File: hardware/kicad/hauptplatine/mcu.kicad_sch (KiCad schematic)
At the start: 31 parts, among them J301 USB-C, J302 Debug (SWD + Serial1), SW301 Reset, SW302 BOOT, SW303 Service, SW304 Reedkontakt, U301 STM32F411CEU6, U302 USBLC6-2SC6, Y301 25MHz 12pF, Y302 32,768k 7pF

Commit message: update
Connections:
- net DBG_RX: now also J302.7 (Pin_7); no longer J302.6 (Pin_6)
- net DBG_TX: now also J302.6 (Pin_6); no longer J302.5 (Pin_5)
- net GND: now also J302.5 (Pin_5); no longer J302.7 (Pin_7)
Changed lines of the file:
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@@
 	(wire
 		(pts
-			(xy 289.56 124.46) (xy 299.72 124.46)
+			(xy 289.56 127) (xy 299.72 127)
 		)
 		(stroke
@@
 	(wire
 		(pts
-			(xy 289.56 121.92) (xy 299.72 121.92)
+			(xy 289.56 124.46) (xy 299.72 124.46)
 		)
 		(stroke
@@
 	)
 	(label "DBG_TX"
-		(at 289.56 121.92 180)
+		(at 289.56 124.46 180)
 		(effects
 			(font
@@
 	)
 	(label "DBG_RX"
-		(at 289.56 124.46 180)
+		(at 289.56 127 180)
 		(effects
 			(font
@@
 	(symbol
 		(lib_id "power:GND")
-		(at 299.72 127 270)
+		(at 299.72 121.92 270)
 		(unit 1)
 		(body_style 1)
@@
 		(dnp no)
 		(property "Reference" "#PWR3031"
-			(at 299.72 127 0)
+			(at 299.72 121.92 0)
 			(hide yes)
 			(show_name no)
@@
 		)
 		(property "Value" "GND"
-			(at 299.72 130.2 0)
+			(at 299.72 125.12 0)
 			(show_name no)
 			(do_not_autoplace no)
@@
 		)
 		(property "Footprint" ""
-			(at 299.72 127 0)
+			(at 299.72 121.92 0)
 			(hide yes)
 			(show_name no)
@@
 		)
 		(property "Datasheet" ""
-			(at 299.72 127 0)
+			(at 299.72 121.92 0)
 			(hide yes)
 			(show_name no)
@@
 		)
 		(property "Description" ""
-			(at 299.72 127 0)
+			(at 299.72 121.92 0)
 			(show_name no)
 			(do_not_autoplace no)
@@
 			)
 		)
-		(property "Description" ""
+		(property "Description" "= J10 in anschluesse.md: 1 3V3, 2 SWDIO, 3 SWCLK, 4 NRST, 5 GND, 6 TX1 (PA9, Ausgang), 7 RX1 (PA10)"
 			(at 304.8 119.38 0)
 			(hide yes)

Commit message: update
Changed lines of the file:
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@@
-		)
-	)
-	(label "DBG_TX"
-		(at 289.56 124.46 180)
-		(effects
-			(font
-				(size 1.27 1.27)
-			)
-			(justify right bottom)
 		)
 	)
@@
 		)
 	)
-	(label "DBG_TX"
-		(at 226.06 127 0)
-		(effects
-			(font
-				(size 1.27 1.27)
-			)
-			(justify left bottom)
-		)
-	)
 	(label "USB_CC1"
 		(at 292.1 214.63 90)
@@
 		)
 	)
-	(label "DBG_RX"
-		(at 226.06 129.54 0)
-		(effects
-			(font
-				(size 1.27 1.27)
-			)
-			(justify left bottom)
-		)
-	)
 	(label "VDDA"
 		(at 207.01 81.28 0)
@@
 		)
 	)
-	(label "DBG_RX"
-		(at 289.56 127 180)
-		(effects
-			(font
-				(size 1.27 1.27)
-			)
-			(justify right bottom)
-		)
-	)
 	(label "BOOT1"
 		(at 86.36 151.13 90)
@@
 		)
 	)
+	(global_label "DBG_TX"
+		(shape bidirectional)
+		(at 289.56 124.46 180)
+		(fields_autoplaced yes)
+		(effects
+			(font
+				(size 1.27 1.27)
+			)
+			(justify right)
+		)
+		(property "Intersheetrefs" "${INTERSHEET_REFS}"
+			(at 289.56 124.46 0)
+			(hide yes)
+			(show_name no)
+			(do_not_autoplace no)
+			(effects
+				(font
+					(size 1.27 1.27)
+				)
+			)
+		)
+	)
 	(global_label "LORA_NSS"
 		(shape bidirectional)
@@
 		)
 	)
+	(global_label "DBG_TX"
+		(shape bidirectional)
+		(at 226.06 127 0)
+		(fields_autoplaced yes)
+		(effects
+			(font
+				(size 1.27 1.27)
+			)
+			(justify left)
+		)
+		(property "Intersheetrefs" "${INTERSHEET_REFS}"
+			(at 226.06 127 0)
+			(hide yes)
+			(show_name no)
+			(do_not_autoplace no)
+			(effects
+				(font
+					(size 1.27 1.27)
+				)
+			)
+		)
+	)
 	(global_label "MIC_ADC"
 		(shape bidirectional)
@@
 		)
 	)
+	(global_label "DBG_RX"
+		(shape bidirectional)
+		(at 226.06 129.54 0)
+		(fields_autoplaced yes)
+		(effects
+			(font
+				(size 1.27 1.27)
+			)
+			(justify left)
+		)
+		(property "Intersheetrefs" "${INTERSHEET_REFS}"
+			(at 226.06 129.54 0)
+			(hide yes)
+			(show_name no)
+			(do_not_autoplace no)
+			(effects
+				(font
+					(size 1.27 1.27)
+				)
+			)
+		)
+	)
 	(global_label "EXT_PB13"
 		(shape bidirectional)
@@
 			(hide yes)
 			(show_name no)
+			(do_not_autoplace no)
+			(effects
+				(font
+					(size 1.27 1.27)
+				)
+			)
+		)
+	)
+	(global_label "DBG_RX"
+		(shape bidirectional)
+		(at 289.56 127 180)
+		(fields_autoplaced yes)
+		(effects
+			(font
+				(size 1.27 1.27)
+			)
+			(justify right)
+		)
+		(property "Intersheetrefs" "${INTERSHEET_REFS}"
+			(at 289.56 127 0)
+			(hide yes)
+			(show_name no)

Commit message: Update
HW-03: Distanzhülsen 10 mm, Bauhöhe ≤ 40 mm; Platinendatei logger.kicad_pcb angelegt (121×121 mm, 4 Lagen, Befestigungslöcher, DRC 0); Reedkontakt MRS03-B-3 und LED LTST-S220KGKT mit Footprints. Tests: ERC 0, Pin/Footprint 0 Abweichungen, Netzprüfung 178/178, alle_tests_linux.sh rc=0
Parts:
- D301: value Side-View -> LTST-S220KGKT; footprint LED_SMD:LED_0603_1608Metric -> Bienen:LED_Lite-On_LTST-S220_SideView; LCSC (none) -> C160469
- SW304: value Reedkontakt -> MRS03-B-3; footprint (none) -> Bienen:MiRelay_MRS03_J-Lead_8.5x2.1mm; LCSC (none) -> C41432613
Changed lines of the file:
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@@
 			)
 		)
-		(property "Value" "Reedkontakt"
+		(property "Value" "MRS03-B-3"
 			(at 256.54 76.143 0)
 			(show_name no)
@@
 			)
 		)
-		(property "Footprint" ""
+		(property "Footprint" "Bienen:MiRelay_MRS03_J-Lead_8.5x2.1mm"
 			(at 256.54 78.74 0)
 			(hide yes)
@@
 			)
 		)
-		(property "Description" "an der Platinenkante neben der LED; Teil und Footprint [P]"
+		(property "Description" "MiRelay MRS03-B-3: Reed SMD 8,5 × 2,1 mm, 10–15 AT; an der Platinenkante neben der LED, Längsachse parallel zur Kante; Schaltabstand durch die Wand am Prototyp [P]"
+			(at 256.54 78.74 0)
+			(hide yes)
+			(show_name no)
+			(do_not_autoplace no)
+			(effects
+				(font
+					(size 1.27 1.27)
+				)
+			)
+		)
+		(property "LCSC" "C41432613"
 			(at 256.54 78.74 0)
 			(hide yes)
@@
 			)
 		)
-		(property "Value" "Side-View"
+		(property "Value" "LTST-S220KGKT"
 			(at 109.966 167.081 90)
 			(show_name no)
@@
 			)
 		)
-		(property "Footprint" "LED_SMD:LED_0603_1608Metric"
+		(property "Footprint" "Bienen:LED_Lite-On_LTST-S220_SideView"
 			(at 106.68 165.1 0)
 			(hide yes)
@@
 			)
 		)
-		(property "Description" "seitlich abstrahlend am Rand unter dem Lichtleiter; Teil/Footprint [P]"
+		(property "Description" "Lite-On, seitlich abstrahlend, grün (AlInGaP 574 nm), am Rand vor dem Lichtleiter; mit 1 kΩ ca. 1,3 mA – Helligkeit am Muster prüfen [P]"
 			(at 106.68 165.1 0)
 			(hide yes)
+			(show_name no)
+			(do_not_autoplace no)
+			(effects
+				(font
+					(size 1.27 1.27)
+				)
+			)
+		)
+		(property "LCSC" "C160469"
+			(at 106.68 165.1 0)
+			(hide yes)

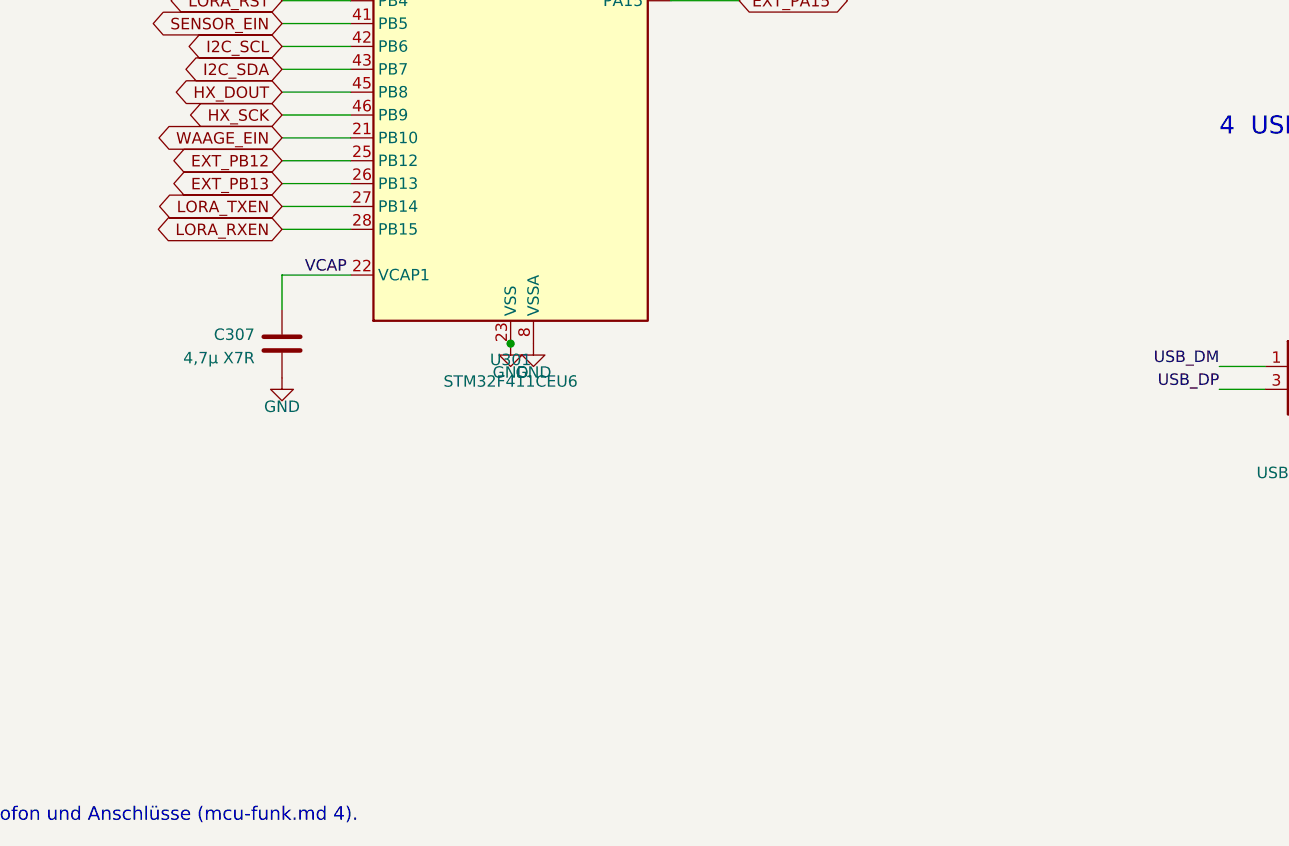
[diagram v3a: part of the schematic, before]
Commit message: HW-06: Akku auf der Hauptplatine (Blatt Akku, Akku-Platine entfällt); HW-05: USB mit VBUS-Erkennung an PB13; Routing-Werkzeuge; Aufräumen: Restbezüge Akku-Platine, README-Stand; ERC 0, Netzprüfung 168/168, Pin/Footprint 0; Platine platziert, nicht geroutet
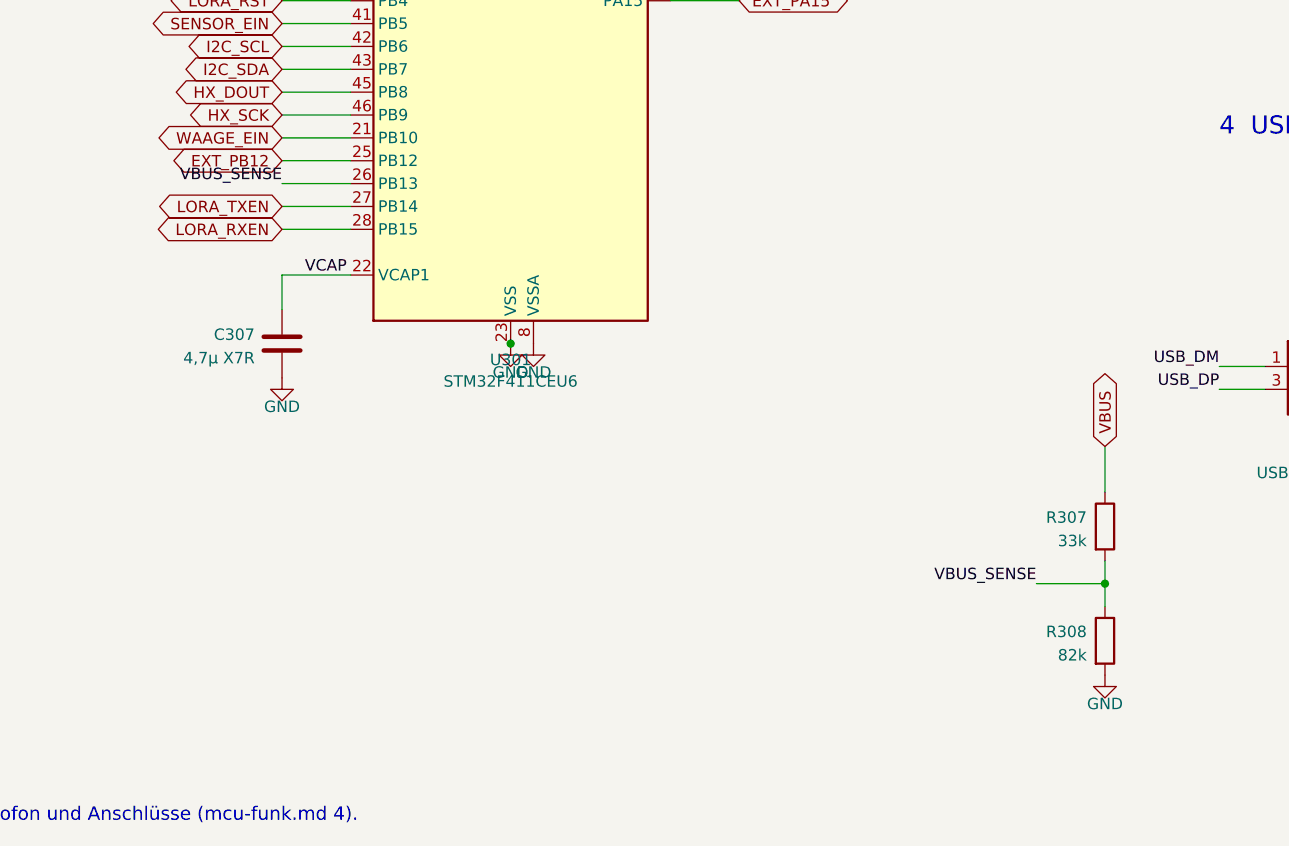
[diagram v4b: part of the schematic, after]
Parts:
- added R307: 33k, Resistor_SMD:R_0603_1608Metric, symbol Device:R
- added R308: 82k, Resistor_SMD:R_0603_1608Metric, symbol Device:R
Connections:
- net GND: now also R308.2
- net VBUS: now also R307.1
- net EXT_PB13 renamed VBUS_SENSE
- net VBUS_SENSE: now also R307.2, R308.1

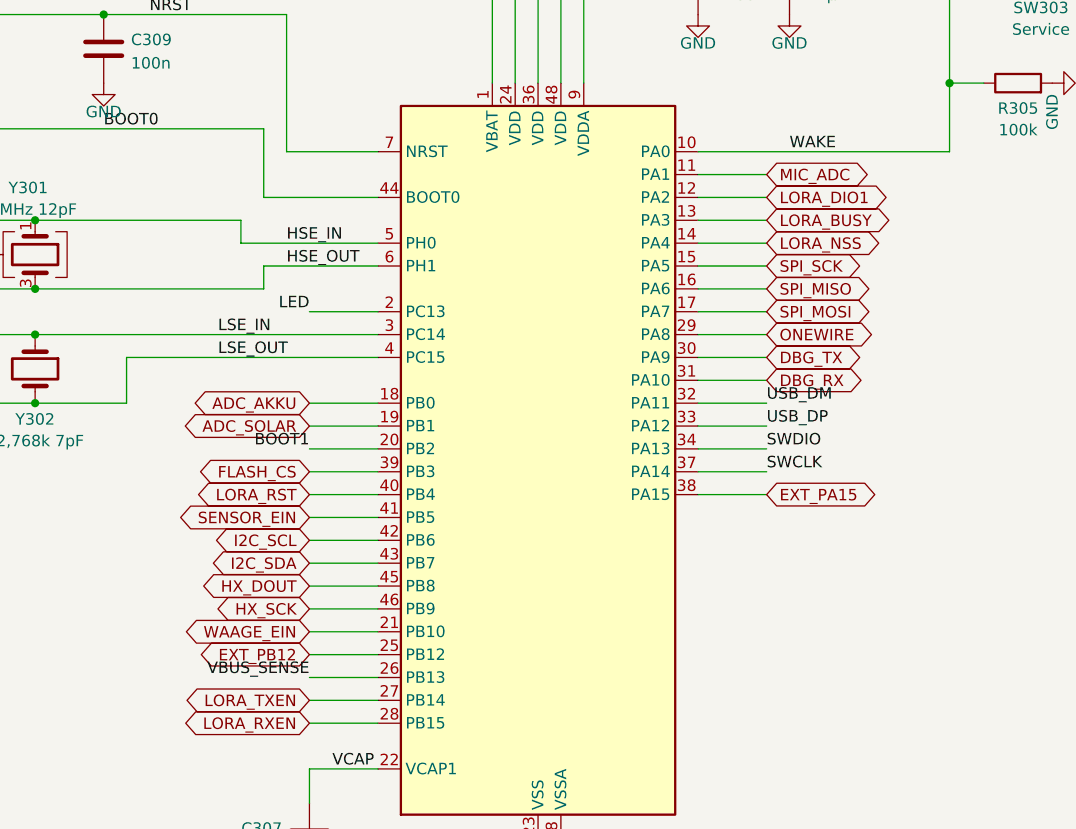
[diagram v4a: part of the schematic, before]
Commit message: HW-07: zwei Mikrofone am Audio-ADC TLV320ADC3101, I2S3, RJ45 J5; HW-08: Platine nur Rahmen, Layout extern; Pflichtenheft und Übergabepaket für den Layouter; ERC 0, Netzprüfung 187/187, Pin/Footprint 0
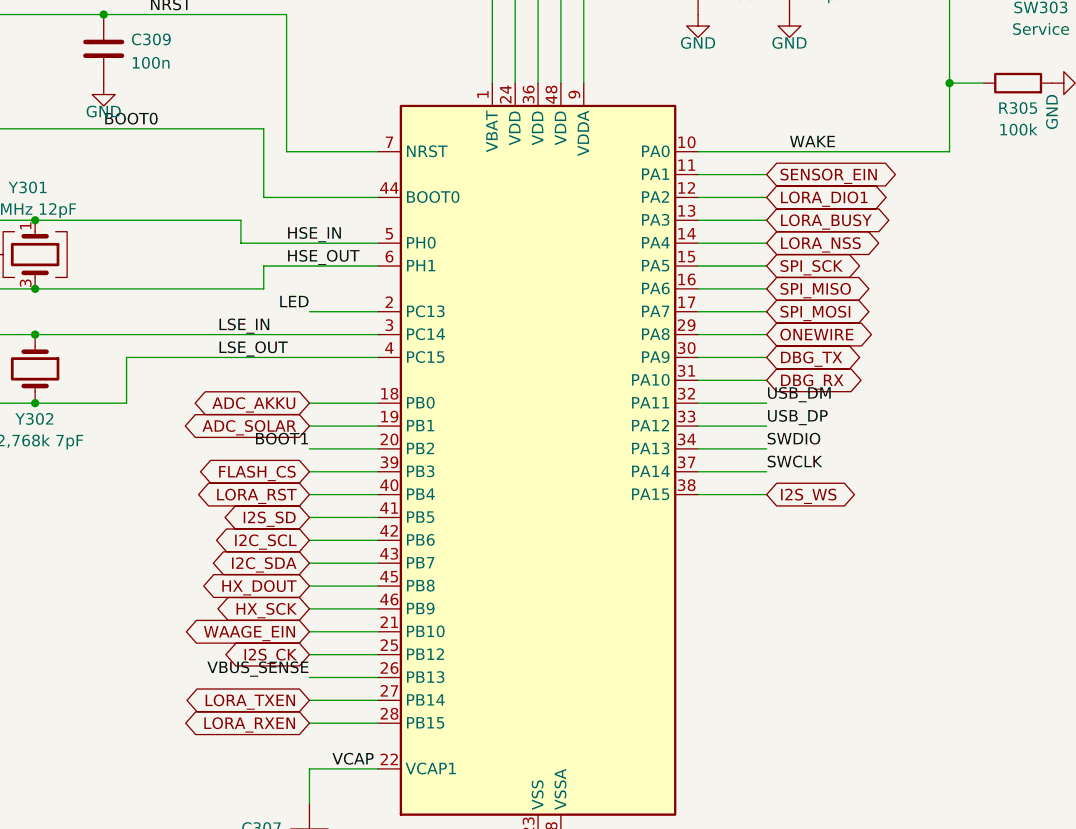
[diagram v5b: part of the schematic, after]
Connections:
- net MIC_ADC is gone; now on net SENSOR_EIN: U301.11 (PA1)
- net SENSOR_EIN: no longer U301.41 (PB5)
- net EXT_PA15 renamed I2S_WS
- net EXT_PB12 renamed I2S_CK
- new net I2S_SD: U301.41 (PB5)
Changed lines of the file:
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@@
 		)
 	)
-	(global_label "EXT_PA15"
+	(global_label "LORA_RST"
+		(shape bidirectional)
+		(at 175.26 142.24 180)
+		(fields_autoplaced yes)
+		(effects
+			(font
+				(size 1.27 1.27)
+			)
+			(justify right)
+		)
+		(property "Intersheetrefs" "${INTERSHEET_REFS}"
+			(at 175.26 142.24 0)
+			(hide yes)
+			(show_name no)
+			(do_not_autoplace no)
+			(effects
+				(font
+					(size 1.27 1.27)
+				)
+			)
+		)
+	)
+	(global_label "I2S_WS"
 		(shape bidirectional)
 		(at 226.06 142.24 0)
@@
 		)
 	)
+	(global_label "LORA_RXEN"
+		(shape bidirectional)
+		(at 175.26 167.64 180)
+		(fields_autoplaced yes)
+		(effects
+			(font
+				(size 1.27 1.27)
+			)
+			(justify right)
+		)
+		(property "Intersheetrefs" "${INTERSHEET_REFS}"
+			(at 175.26 167.64 0)
+			(hide yes)
+			(show_name no)
+			(do_not_autoplace no)
+			(effects
+				(font
+					(size 1.27 1.27)
+				)
+			)
+		)
+	)
+	(global_label "DBG_TX"
+		(shape bidirectional)
+		(at 226.06 127 0)
+		(fields_autoplaced yes)
+		(effects
+			(font
+				(size 1.27 1.27)
+			)
+			(justify left)
+		)
+		(property "Intersheetrefs" "${INTERSHEET_REFS}"
+			(at 226.06 127 0)
+			(hide yes)
+			(show_name no)
+			(do_not_autoplace no)
+			(effects
+				(font
+					(size 1.27 1.27)
+				)
+			)
+		)
+	)
+	(global_label "VBUS"
+		(shape bidirectional)
+		(at 289.56 172.72 90)
+		(fields_autoplaced yes)
+		(effects
+			(font
+				(size 1.27 1.27)
+			)
+			(justify left)
+		)
+		(property "Intersheetrefs" "${INTERSHEET_REFS}"
+			(at 289.56 172.72 0)
+			(hide yes)
+			(show_name no)
+			(do_not_autoplace no)
+			(effects
+				(font
+					(size 1.27 1.27)
+				)
+			)
+		)
+	)
+	(global_label "I2S_CK"
+		(shape bidirectional)
+		(at 175.26 160.02 180)
+		(fields_autoplaced yes)
+		(effects
+			(font
+				(size 1.27 1.27)
+			)
+			(justify right)
+		)
+		(property "Intersheetrefs" "${INTERSHEET_REFS}"
+			(at 175.26 160.02 0)
+			(hide yes)
+			(show_name no)
+			(do_not_autoplace no)
+			(effects
+				(font
+					(size 1.27 1.27)
+				)
+			)
+		)
+	)
+	(global_label "VBUS"
+		(shape bidirectional)
+		(at 314.96 208.28 180)
+		(fields_autoplaced yes)
+		(effects
+			(font
+				(size 1.27 1.27)
+			)
+			(justify right)
+		)
+		(property "Intersheetrefs" "${INTERSHEET_REFS}"
+			(at 314.96 208.28 0)
+			(hide yes)
+			(show_name no)
+			(do_not_autoplace no)
+			(effects
+				(font
+					(size 1.27 1.27)
+				)
+			)
+		)
+	)
+	(global_label "I2S_SD"
+		(shape bidirectional)
+		(at 175.26 144.78 180)
+		(fields_autoplaced yes)
+		(effects
+			(font
+				(size 1.27 1.27)
+			)
+			(justify right)
+		)
+		(property "Intersheetrefs" "${INTERSHEET_REFS}"
+			(at 175.26 144.78 0)
+			(hide yes)
+			(show_name no)
+			(do_not_autoplace no)
+			(effects
+				(font
+					(size 1.27 1.27)
+				)
+			)
+		)
+	)
 	(global_label "SENSOR_EIN"
 		(shape bidirectional)
-		(at 175.26 144.78 180)
-		(fields_autoplaced yes)
-		(effects
-			(font
-				(size 1.27 1.27)
-			)
-			(justify right)
-		)
-		(property "Intersheetrefs" "${INTERSHEET_REFS}"
-			(at 175.26 144.78 0)
-			(hide yes)
-			(show_name no)
-			(do_not_autoplace no)
-			(effects
-				(font
-					(size 1.27 1.27)
-				)
-			)
-		)
-	)
-	(global_label "LORA_RST"
-		(shape bidirectional)
-		(at 175.26 142.24 180)
-		(fields_autoplaced yes)
-		(effects
-			(font
-				(size 1.27 1.27)
-			)
-			(justify right)
-		)
-		(property "Intersheetrefs" "${INTERSHEET_REFS}"
-			(at 175.26 142.24 0)
-			(hide yes)
-			(show_name no)
-			(do_not_autoplace no)
-			(effects
-				(font
-					(size 1.27 1.27)
-				)
-			)
-		)
-	)
-	(global_label "LORA_RXEN"
-		(shape bidirectional)
-		(at 175.26 167.64 180)
-		(fields_autoplaced yes)
-		(effects
-			(font
-				(size 1.27 1.27)
-			)
-			(justify right)
-		)
-		(property "Intersheetrefs" "${INTERSHEET_REFS}"
-			(at 175.26 167.64 0)
-			(hide yes)
-			(show_name no)
-			(do_not_autoplace no)
-			(effects
-				(font
-					(size 1.27 1.27)
-				)
-			)
-		)
-	)
-	(global_label "DBG_TX"
-		(shape bidirectional)
-		(at 226.06 127 0)
-		(fields_autoplaced yes)
-		(effects
-			(font
-				(size 1.27 1.27)
-			)
-			(justify left)
-		)
-		(property "Intersheetrefs" "${INTERSHEET_REFS}"
-			(at 226.06 127 0)
-			(hide yes)
-			(show_name no)
-			(do_not_autoplace no)
-			(effects
-				(font
-					(size 1.27 1.27)
-				)
-			)
-		)
-	)
-	(global_label "MIC_ADC"
-		(shape bidirectional)
 		(at 226.06 106.68 0)
 		(fields_autoplaced yes)
@@
 		)
 	)
-	(global_label "VBUS"
-		(shape bidirectional)
-		(at 289.56 172.72 90)
-		(fields_autoplaced yes)
-		(effects
-			(font
-				(size 1.27 1.27)
-			)
-			(justify left)
-		)
-		(property "Intersheetrefs" "${INTERSHEET_REFS}"
-			(at 289.56 172.72 0)
-			(hide yes)
-			(show_name no)
-			(do_not_autoplace no)
-			(effects
-				(font
-					(size 1.27 1.27)
-				)
-			)
-		)
-	)
-	(global_label "VBUS"
-		(shape bidirectional)
-		(at 314.96 208.28 180)
-		(fields_autoplaced yes)
-		(effects
-			(font
-				(size 1.27 1.27)
-			)
-			(justify right)
-		)
-		(property "Intersheetrefs" "${INTERSHEET_REFS}"
-			(at 314.96 208.28 0)
-			(hide yes)
-			(show_name no)
-			(do_not_autoplace no)
-			(effects
-				(font
-					(size 1.27 1.27)
-				)
-			)
-		)
-	)
 	(global_label "DBG_RX"
 		(shape bidirectional)
@@
 			(hide yes)
 			(show_name no)
-			(do_not_autoplace no)
-			(effects
-				(font
-					(size 1.27 1.27)
-				)
-			)
-		)
-	)
-	(global_label "EXT_PB12"
-		(shape bidirectional)
-		(at 175.26 160.02 180)
-		(fields_autoplaced yes)
-		(effects
-			(font
-				(size 1.27 1.27)
-			)
-			(justify right)
-		)
-		(property "Intersheetrefs" "${INTERSHEET_REFS}"
-			(at 175.26 160.02 0)
-			(hide yes)
-			(show_name no)
